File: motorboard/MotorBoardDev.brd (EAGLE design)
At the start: 93.5 x 80.5 mm, 88 parts, among them J1 Under Glow, J2 Safety Light, J3 12V, J4 24V, Q1 TIP42C, Q10 TIP42C, Q11 TIP42C, Q15 TIP41C, Q16 TIP41C, Q2 220mA/50V/3.5Ω, Q3 TIP42C, Q4 TIP42C, Q5 TIP42C, Q6 TIP42C, Q7 220mA/50V/3.5Ω, Q8 220mA/50V/3.5Ω, Q9 220mA/50V/3.5Ω, T1 NCP1117DT50GOS-ND, T2 TIP41A, T3 NCP1117DT33GOS-ND, U2 9DoF IMU, X1 C-GRID-05-15-91, X2 C-GRID-05-15-91, X3 MINI-USB_SHIELD5P4-32005-400, X4 C-GRID-02-70553, X5 SI-50170, X7 2510-, X8 2510-

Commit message: Magic
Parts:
- removed Q2, Q7, Q8, Q9: 220mA/50V/3.5Ω, SparkFun-DiscreteSemi:SOT23-3
- removed R31, R32, R33, R34, R35, R36, R37, R38: 10k, SparkFun-Resistors:0603
- added D5: BLUE, SparkFun-LED:LED-0603
- added U1: TXB0104DR, MotorBoardDev:D14
- D3: value WHITE -> Yellow
- R10: value 200 -> 4.7k
- R16: value 200 -> 500
- R21, R22, R23, R24: value 1k -> 30
- R25, R27, R28, R29: value 10k -> 4.7k
- moved D3 0.25 mm to (12.0, 17.8)
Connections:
- net D+ renamed D_P
- net D- renamed D_N
- net RD+ renamed RD_P
- net RD- renamed RD_N
- net TD+ renamed TD_P
- net TD- renamed TD_N
- removed net ID: X3.4
- removed net LSPEED: A1.25, R21.1
- removed net N$37: A1.30, R39.1
- removed net N$38: A1.29, R40.1
- new net LALI_CTRL: A1.23, R21.1
- new net LBLI_CTRL: R23.1
- new net N$17: X7.4
- new net N$18: X7.3
- new net N$7: J2.2, T2.3
- new net RALI_CTRL: R22.1
- new net RBLI_CTRL: R24.1
- net +3V3: now also U1.14; no longer Q2.1, Q7.1, Q8.1, Q9.1, R32.2, R33.2, R35.2, R37.2
- net +5V: now also U1.1; no longer R31.2, R34.2, R36.2, R38.2
- net BLUE: no longer A1.21
- net ESTOP: now also A1.22; no longer A1.24
- net GND: now also D5.C, U1.7, U1.8; no longer J1.4, J1.8, J1.9, J2.2
- net GREEN: no longer A1.22
- net INDICATOR_LED: now also D5.A
- net LDIR: now also A1.24; no longer A1.26, R23.1
- net LEA: now also U1.2; no longer Q2.3, R31.1
- net LEA3: now also U1.13; no longer Q2.2, R32.1
- net LEB: now also U1.3; no longer Q8.3, R36.1
- net LEB3: now also U1.12; no longer Q8.2, R37.1
- net N$1: no longer T2.3
- net RDIR: now also A1.26; no longer A1.28, R24.1
- net REA: now also U1.4; no longer Q7.3, R34.1
- net REA3: now also U1.11; no longer Q7.2, R33.1
- net REB: now also U1.5; no longer Q9.3, R38.1
- net REB3: now also U1.10; no longer Q9.2, R35.1
- net RED: no longer A1.23
- net RSPEED: now also A1.25; no longer A1.27, R22.1
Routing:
- net +3V3: track 57.9 -> 0.00 mm, vias 5 -> 0
- net RDIR: track 55.8 -> 0.00 mm, vias 1 -> 0
- net RBLI_CTRL: track 0.00 -> 51.0 mm, vias 0 -> 1
- net RSPEED: track 48.7 -> 0.00 mm, vias 1 -> 0
- net RALI_CTRL: track 0.00 -> 48.6 mm, vias 0 -> 1
- net LDIR: track 32.1 -> 0.00 mm, vias 1 -> 0
- net LBLI_CTRL: track 0.00 -> 32.0 mm, vias 0 -> 1
- net LSPEED: track 27.4 -> 0.00 mm, vias 1 -> 0
- net LALI_CTRL: track 0.00 -> 24.7 mm, vias 0 -> 1
- net RD_N: track 21.1 -> 9.40 mm
- net RD_P: track 21.1 -> 9.44 mm
- net TD_N: track 20.1 -> 11.1 mm
- net REA: track 14.5 -> 8.28 mm
- net LEA: track 18.5 -> 12.3 mm
- net REB: track 11.4 -> 5.17 mm
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
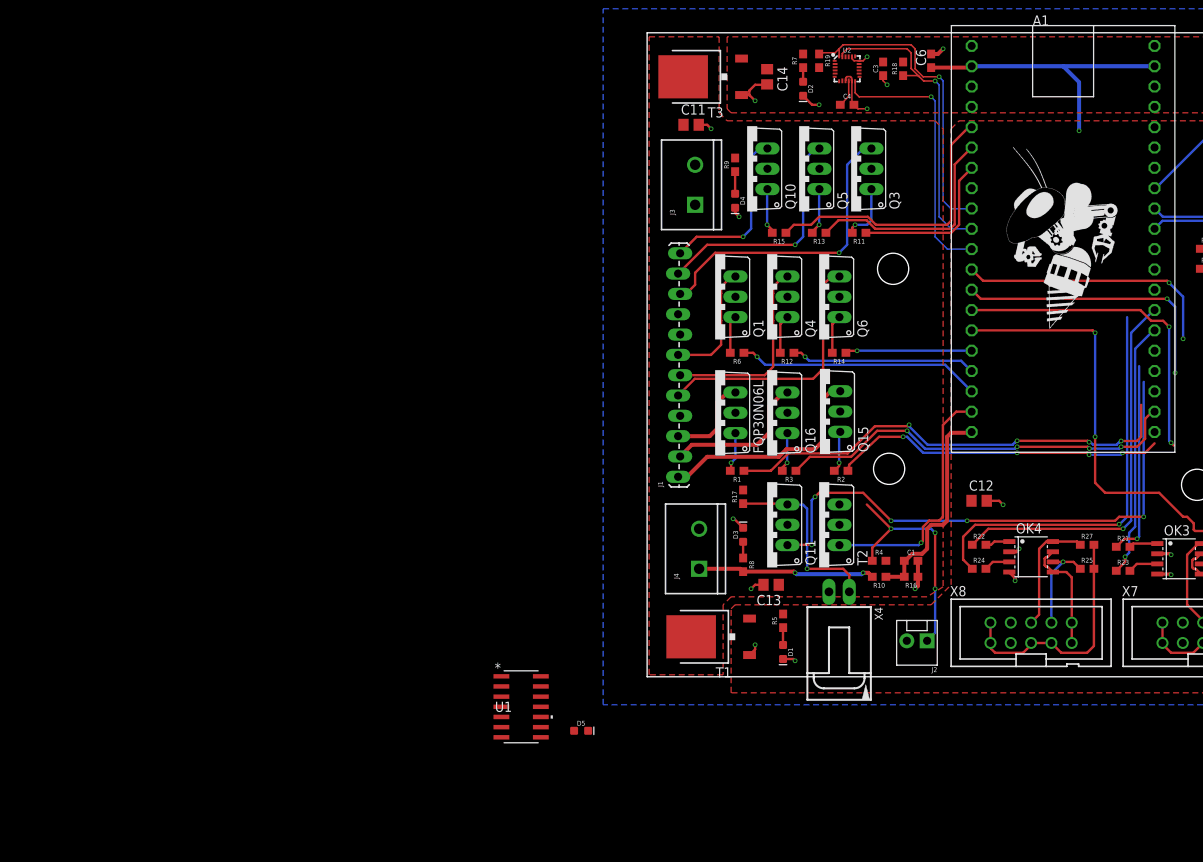
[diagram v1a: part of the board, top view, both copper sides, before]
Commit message: Changes so far so Ryan3 can complete BOM
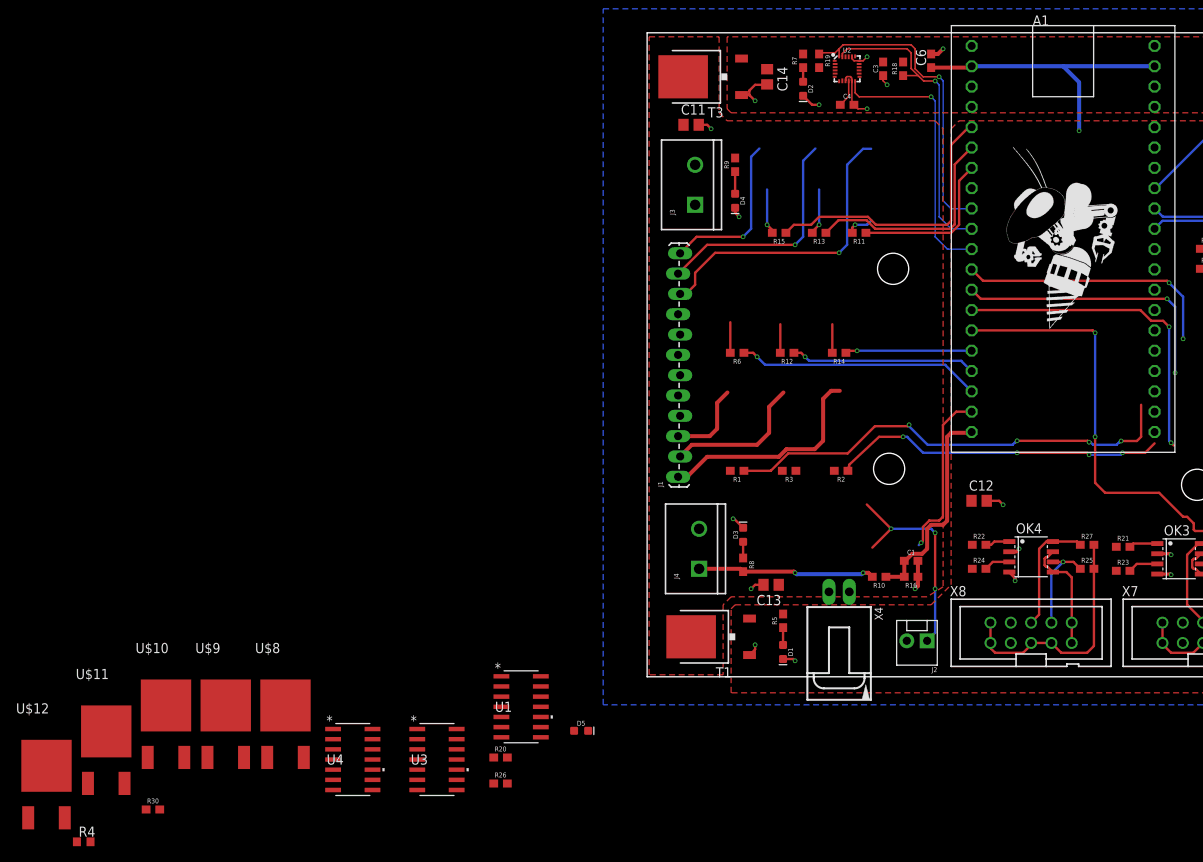
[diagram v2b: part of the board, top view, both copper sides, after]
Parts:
- removed FQP30N06L, Q15, Q16: TIP41C, transistor-power:TO220AV
- removed Q1, Q10, Q11, Q3, Q4, Q5, Q6: TIP42C, transistor-power:TO220AV
- removed R17: 2700, SparkFun-Resistors:0603
- removed T2: TIP41A, transistor:TO220V
- added R20, R26: 1k, SparkFun-Resistors:0603
- added R30: 2700, SparkFun-Resistors:0603
- added U$10, U$11, U$12, U$8, U$9: STD10P6F6, MotorBoardDev:STD10P6F6_DPAK
- added U3, U4: TXB0104DR, MotorBoardDev:D14
- R4: value 2700 -> (none); device SparkFun-Resistors:0603 -> rcl:R0603
- moved R4 105.4 mm to (-70.4, -20.6)
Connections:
- removed net LDIR: A1.24
- removed net RDIR: A1.26
- removed net RSPEED: A1.25
- new net LDISABLE: R20.2, X7.4
- new net N$19: R3.2, U$9.GATE
- new net RDISABLE: R26.2, X8.4
- new net VCCA: U3.1, U4.1
- new net VCCB: U3.14, U4.14
- net +12V: now also U$10.DRAIN, U$11.DRAIN, U$12.DRAIN, U$8.DRAIN, U$9.DRAIN; no longer FQP30N06L.C, Q15.C, Q16.C, R17.2, R4.2
- net 1S1O: now also J1.4; no longer J1.7, Q1.E
- net 1S2O: now also J1.5; no longer J1.6, Q4.E
- net 1S3O: now also J1.6; no longer J1.5, Q6.E
- net 2S1O: no longer Q3.E
- net 2S2O: no longer Q5.E
- net 2S3O: no longer Q10.E
- net BLUE: now also A1.29
- net BLUE_OUT: now also U$10.SOURCE; no longer Q15.E
- net ESTOP: now also A1.27, R4.1; no longer A1.22, Q11.B
- net GND: now also J2.2, U3.7, U4.7; no longer Q1.C, Q10.C, Q11.C, Q3.C, Q4.C, Q5.C, Q6.C, T2.2
- net GREEN: now also A1.28
- net GREEN_OUT: now also U$9.SOURCE; no longer Q16.E
- net LBLI_CTRL: now also A1.24
- net LGND: now also R20.1
- net N$1: now also U$11.SOURCE; no longer R4.1
- net N$10: now also U$12.SOURCE, X4.1; no longer Q16.B, R3.2
- net N$11: no longer Q6.B
- net N$13: no longer Q4.B
- net N$14: no longer Q1.B
- net N$15: no longer Q3.B
- net N$16: no longer Q5.B
- net N$17: now also A1.22, R39.1; no longer X7.4
- net N$18: now also A1.21, R40.1; no longer X7.3
- net N$28: no longer Q10.B
- net N$3: now also U$8.GATE; no longer FQP30N06L.B
- net N$4: now also U$10.GATE; no longer Q15.B
- net N$7: now also R30.1, U$11.GATE; no longer J2.2, T2.3
- net N$8: now also R4.2, U$12.GATE; no longer Q11.E, R17.1, X4.1
- net RALI_CTRL: now also A1.25
- net RBLI_CTRL: now also A1.26
- net RED: now also A1.30
- net RED_OUT: now also U$8.SOURCE; no longer FQP30N06L.E
- net RGND: now also R26.1
- net SAFETY_LIGHT: now also R30.2; no longer T2.1
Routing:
- net ESTOP: track 69.0 -> 0.00 mm, vias 5 -> 0
- net GREEN: track 51.1 -> 0.00 mm, vias 4 -> 0
- net RBLI_CTRL: track 51.0 -> 0.00 mm, vias 1 -> 0
- net RALI_CTRL: track 48.6 -> 0.00 mm, vias 1 -> 0
- net 1S3O: track 32.5 -> 0.00 mm
- net LBLI_CTRL: track 32.0 -> 0.00 mm, vias 1 -> 0
- net LALI_CTRL: track 24.7 -> 0.00 mm, vias 1 -> 0
- net 1S2O: track 24.4 -> 0.00 mm
- net N$8: track 23.5 -> 0.00 mm, vias 1 -> 0
- net 1S1O: track 15.5 -> 0.00 mm
- net SAFETY_LIGHT: track 31.2 -> 21.3 mm
- net N$4: track 5.18 -> 0.00 mm, vias 1 -> 0
- net N$10: track 4.98 -> 0.00 mm, vias 1 -> 0
- net N$3: track 4.98 -> 0.00 mm, vias 1 -> 0
- net N$15: track 7.33 -> 3.41 mm
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
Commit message: Motor board updated after design review
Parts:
- removed R11, R12, R13, R14, R15, R6: 200, SparkFun-Resistors:0603
- removed T1: NCP1117DT50GOS-ND, IGVC-Regulators:TO252
- removed T3: NCP1117DT33GOS-ND, IGVC-Regulators:TO252
- removed U$10, U$11, U$12: STD10P6F6, MotorBoardDev:STD10P6F6_DPAK
- added Q1, Q2, Q3: SSM3J338R, RoboJackets-Discrete:SOT-23-3
- added Q4: STT4P3LLH6, MotorBoardDev:SOT23-6
- C14: value 10uF -> 1uF
- J2: value Safety Light -> B2PS-VH(LF)(SN); device SparkFun-Retired:MOLEX-1X2 -> RoboJackets-Connectors:B2PS-CENTERED
- J3: value 12V -> B2PS-VH(LF)(SN); device SparkFun-Connectors:SCREWTERMINAL-5MM-2 -> RoboJackets-Connectors:B2PS-CENTERED
- J4: value 24V -> B2PS-VH(LF)(SN); device SparkFun-Connectors:SCREWTERMINAL-5MM-2 -> RoboJackets-Connectors:B2PS-CENTERED
- U$8: value STD10P6F6 -> RRH100P03GZETB; device MotorBoardDev:STD10P6F6_DPAK -> MotorBoardDev:SOIC-8
- U$9: value STD10P6F6 -> R-78E5.0-1.0; device MotorBoardDev:STD10P6F6_DPAK -> MotorBoardDev:R-78E
- U3: value TXB0104DR -> TXB0106PWR; device MotorBoardDev:D14 -> MotorBoardDev:PW16
- U4: value TXB0104DR -> TLV70233DBVR; device MotorBoardDev:D14 -> RoboJackets-PowerICs:SOT-23-5
- moved J2 183.3 mm to (-90.0, -129.5), turned to 0 degrees
- moved U$9 166.5 mm to (-98.5, -166.0)
- moved U4 159.7 mm to (-106.5, -154.0)
- moved J3 149.0 mm to (-65.0, -72.0), turned to 0 degrees
- moved J4 131.6 mm to (-65.0, -97.0), turned to 0 degrees
- moved U3 114.3 mm to (-74.5, -114.0)
- moved U$8 19.6 mm to (-37.5, -24.0)
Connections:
- removed net 1S1: A1.18, R6.1
- removed net 1S1O: J1.4
- removed net 1S2: A1.17, R12.1
- removed net 1S2O: J1.5
- removed net 1S3: A1.16, R14.1
- removed net 1S3O: J1.6
- removed net 2S1: A1.7, R11.1
- removed net 2S1O: J1.10
- removed net 2S2: A1.6, R13.1
- removed net 2S2O: J1.11
- removed net 2S3: A1.5, R15.1
- removed net 2S3O: J1.12
- removed net ESTOP: A1.27, R4.1
- removed net N$11: R14.2
- removed net N$13: R12.2
- removed net N$14: R6.2
- removed net N$15: R11.2
- removed net N$16: R13.2
- removed net N$28: R15.2
- removed net N$3: R1.2, U$8.GATE
- removed net VCCA: U3.1, U4.1
- removed net VCCB: U3.14, U4.14
- new net BLUE_3V3: A1.29, U3.4
- new net FRONT_LIGHT: R4.1, U3.12
- new net FRONT_LIGHT_3V3: A1.27, U3.5
- new net GREEN_3V3: A1.28, U3.3
- new net N$26: Q1.1, R1.2
- new net RED_3V3: A1.30, U3.1
- new net SAFETY_LIGHT_3V3: A1.19, U3.6
- net +12V: now also J3.2, Q1.2, Q2.2, Q3.2, Q4.4, U$8.1, U$8.2, U$8.3, U$9.1; no longer C13.1, J3.1, T1.3, T3.3, U$10.DRAIN, U$11.DRAIN, U$12.DRAIN, U$8.DRAIN, U$9.DRAIN
- net +24V: now also J4.2; no longer J4.1
- net +3V3: now also U3.2, U4.5; no longer T3.2
- net +5V: now also C13.1, U$9.3, U3.15, U4.1, U4.3; no longer T1.2
- net BLUE: now also U3.13; no longer A1.29
- net BLUE_OUT: now also Q3.3; no longer U$10.SOURCE
- net GND: now also J1.10, J1.11, J1.12, J1.4, J1.5, J1.6, J3.1, J4.1, U$9.2, U3.9, U4.2; no longer J2.2, J3.2, J4.2, T1.1, T3.1, U3.7, U4.7
- net GREEN: now also U3.14; no longer A1.28
- net GREEN_OUT: now also Q2.3; no longer U$9.SOURCE
- net N$1: now also J2.2, Q4.1, Q4.2, Q4.5, Q4.6; no longer J2.1, U$11.SOURCE
- net N$10: now also U$8.5, U$8.6, U$8.7, U$8.8; no longer U$12.SOURCE
- net N$19: now also Q2.1; no longer U$9.GATE
- net N$4: now also Q3.1; no longer U$10.GATE
- net N$7: now also Q4.3; no longer U$11.GATE
- net N$8: now also U$8.4; no longer U$12.GATE
- net RED: now also U3.16; no longer A1.30
- net RED_OUT: now also Q1.3; no longer U$8.SOURCE
- net SAFETY_LIGHT: now also U3.11; no longer A1.19
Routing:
- net 2S1O: track 38.1 -> 0.00 mm, vias 1 -> 0
- net 2S3: track 35.1 -> 0.00 mm
- net 1S1: track 30.5 -> 0.00 mm, vias 1 -> 0
- net 2S2O: track 29.2 -> 0.00 mm, vias 1 -> 0
- net 2S2: track 27.9 -> 0.00 mm
- net N$1: track 27.2 -> 0.00 mm, vias 3 -> 0
- net 1S2: track 23.2 -> 0.00 mm, vias 1 -> 0
- net SAFETY_LIGHT_3V3: track 0.00 -> 21.3 mm, vias 0 -> 1
- net SAFETY_LIGHT: track 21.3 -> 0.00 mm, vias 1 -> 0
- net 2S3O: track 20.6 -> 0.00 mm, vias 1 -> 0
- net 2S1: track 19.8 -> 0.00 mm
- net 1S3: track 15.8 -> 0.00 mm, vias 1 -> 0
- net N$16: track 5.77 -> 0.00 mm, vias 1 -> 0
- net N$28: track 5.69 -> 0.00 mm, vias 1 -> 0
- net +24V: track 22.2 -> 17.1 mm
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
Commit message: added value to R4
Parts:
- R4: value (none) -> 2.7k
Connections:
- net GND: now also J2.1
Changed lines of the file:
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@@
 <attribute name="PROD_ID" value="RES-08701" x="-61.77" y="-16.585" size="1.778" layer="27" display="off"/>
 </element>
-<element name="R4" library="rcl" library_urn="urn:adsk.eagle:library:334" package="R0603" package3d_urn="urn:adsk.eagle:package:23555/2" value="" x="-70.425" y="-20.625"/>
+<element name="R4" library="rcl" library_urn="urn:adsk.eagle:library:334" package="R0603" package3d_urn="urn:adsk.eagle:package:23555/2" value="2.7k" x="-70.425" y="-20.625"/>
 <element name="J3" library="RoboJackets-Connectors" package="B2PS-CENTERED" value="B2PS-VH(LF)(SN)" x="-65" y="-72">
 <attribute name="DIGIKEY" value="455-1648-ND" x="-65" y="-72" size="1.778" layer="27" display="off"/>
@@
 <contactref element="U4" pad="2"/>
 <contactref element="U$9" pad="2"/>
+<contactref element="J2" pad="1"/>
+<wire x1="-71.6806" y1="-116.275" x2="-91.98" y2="-129.5" width="0" layer="19" extent="1-1"/>
 <wire x1="-66.98" y1="-97" x2="-71.6806" y2="-116.275" width="0" layer="19" extent="1-1"/>
 <wire x1="-66.98" y1="-72" x2="-66.98" y2="-97" width="0" layer="19" extent="1-1"/>
-<wire x1="-106.5" y1="-155.306" x2="-71.6806" y2="-116.275" width="0" layer="19" extent="1-1"/>
+<wire x1="-106.5" y1="-155.306" x2="-91.98" y2="-129.5" width="0" layer="19" extent="1-1"/>
 <wire x1="-98.5" y1="-166" x2="-106.5" y2="-155.306" width="0" layer="19" extent="1-1"/>
 <wire x1="-18.2138" y1="-7.56" x2="-66.98" y2="-72" width="0" layer="19" extent="1-1"/>

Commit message: Routing Finished, differential pair and silkscreen still need to be fixed.
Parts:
- added R6: 100, rcl:R0603
- moved U4 274.4 mm to (52.0, 70.0)
- moved U$9 243.0 mm to (32.0, 39.0), turned to 90 degrees
- moved Q4 241.5 mm to (12.0, 68.5), turned to 270 degrees
- moved J2 231.2 mm to (16.0, 76.0), turned to 270 degrees
- moved U3 183.6 mm to (19.0, 44.0), turned to 270 degrees
- moved Q1 177.8 mm to (17.5, 34.5), turned to 90 degrees
- moved Q2 176.5 mm to (17.5, 29.5), turned to 90 degrees
- moved Q3 175.5 mm to (17.5, 24.5), turned to 90 degrees
- moved J3 155.7 mm to (16.0, 61.0), turned to 270 degrees
- moved J4 140.0 mm to (17.0, 16.5), turned to 270 degrees
- moved R30 115.9 mm to (18.0, 67.5)
- moved R4 105.3 mm to (27.5, 18.0)
- moved U1 97.0 mm to (70.8, 40.2), turned to 180 degrees
- moved R20 81.0 mm to (59.5, 12.5)
- moved D5 79.8 mm to (34.0, 61.0), turned to 180 degrees
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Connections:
- net RD_N renamed RD-
- net RD_P renamed RD+
- new net N$3: D5.C, R6.2
- net BLUE_3V3: now also A1.28; no longer A1.29
- net GND: now also R6.1; no longer D5.C
- net GREEN_3V3: now also A1.29; no longer A1.28
- net LEA: now also U1.3; no longer U1.2
- net LEA3: now also U1.12; no longer U1.13
- net LEB: now also U1.2; no longer U1.3
- net LEB3: now also U1.13; no longer U1.12
- net REA: now also U1.5; no longer U1.4
- net REA3: now also U1.10; no longer U1.11
- net REB: now also U1.4; no longer U1.5
- net REB3: now also U1.11; no longer U1.10
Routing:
- net +3V3: track 0.00 -> 66.3 mm, vias 0 -> 5
- net BLUE_3V3: track 0.00 -> 56.4 mm, vias 0 -> 3
- net GREEN_3V3: track 0.00 -> 54.6 mm, vias 0 -> 3
- net RED_3V3: track 0.00 -> 52.3 mm, vias 0 -> 3
- net RED: track 58.0 -> 5.92 mm, vias 4 -> 0
- net FRONT_LIGHT_3V3: track 0.00 -> 47.5 mm, vias 0 -> 3
- net RBLI_CTRL: track 0.00 -> 47.0 mm, vias 0 -> 2
- net RALI_CTRL: track 0.00 -> 40.2 mm, vias 0 -> 2
- net FRONT_LIGHT: track 0.00 -> 30.9 mm, vias 0 -> 2
- net N$17: track 0.00 -> 28.7 mm, vias 0 -> 1
- net SAFETY_LIGHT: track 0.00 -> 28.7 mm, vias 0 -> 4
- net N$18: track 0.00 -> 28.5 mm, vias 0 -> 1
- net LBLI_CTRL: track 0.00 -> 25.7 mm
- net +5V: track 36.9 -> 62.5 mm, vias 1 -> 2
- net BLUE: track 41.9 -> 17.2 mm, vias 4 -> 2
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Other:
- board size 93.5 x 80.5 mm -> 86 x 80.5 mm
